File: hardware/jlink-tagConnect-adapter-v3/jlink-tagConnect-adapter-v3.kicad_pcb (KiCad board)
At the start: 2 copper layers, 48.3 x 30.5 mm, 15 parts, among them J1 Conn_02x10_Odd_Even, J2 Conn_02x05_Odd_Even, J3 Conn_02x05_Odd_Even, J4 Conn_01x03

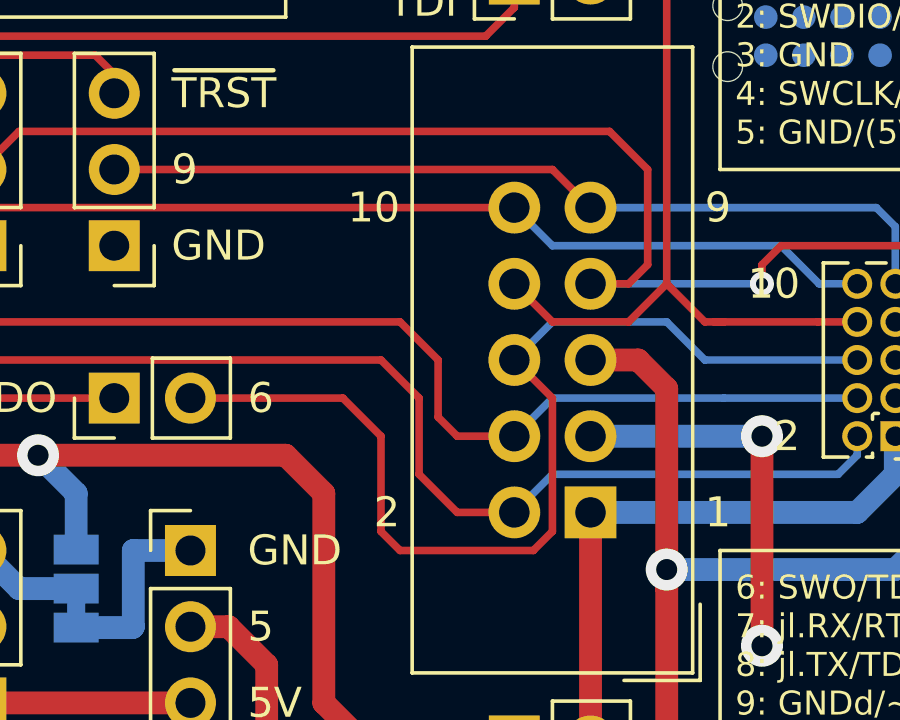
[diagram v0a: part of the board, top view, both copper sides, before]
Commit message: Added JLCPCB order number position
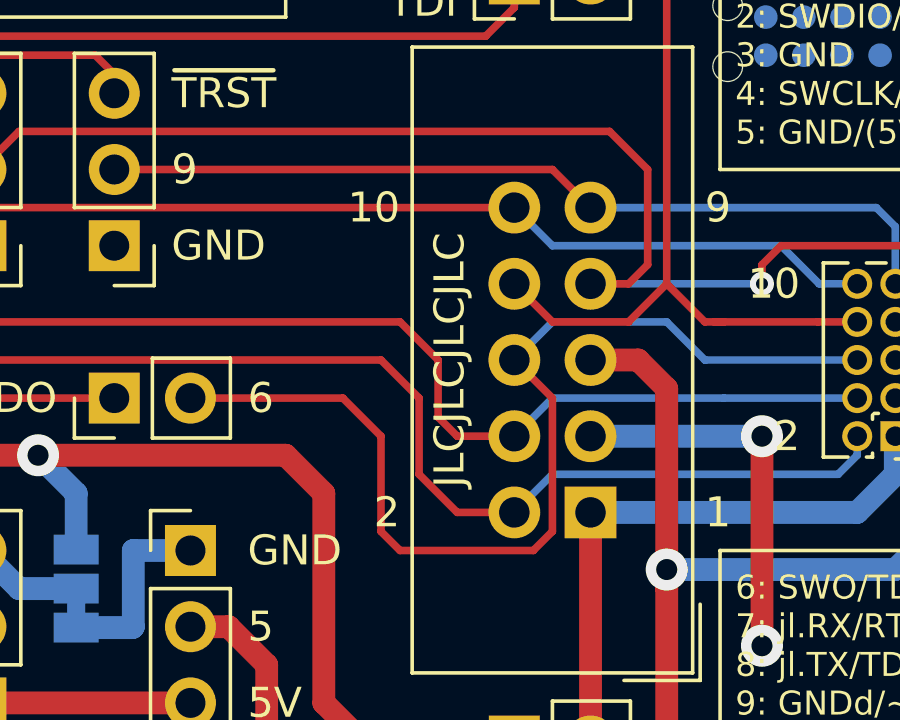
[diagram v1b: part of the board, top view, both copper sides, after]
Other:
- board text added: "JLCJLCJLCJLC"
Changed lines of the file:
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@@
   (general
     (thickness 1.6)
-    (drawings 72)
+    (drawings 73)
     (tracks 169)
     (zones 0)
@@
   )
   (page A4)
+  (title_block
+    (date 2020-12-26)
+  )
   (layers
     (0 F.Cu signal)
@@
     )
   )
+  (gr_text JLCJLCJLCJLC (at 117.856 106.68 90) (layer F.SilkS)
+    (effects (font (size 1 1) (thickness 0.15)))
+  )
   (gr_text "Universal J-Link Adapter" (at 112.395 95.25 90) (layer B.SilkS)
